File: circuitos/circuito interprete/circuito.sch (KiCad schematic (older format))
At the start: 20 parts, among them IC1 ATMEGA328-P, P1 CONN_5V, P10 CONN_LIM_Y, P11 CONN_E_STOP, P2 CONN_02X03, P3 CONN_EJE_X, P4 CONN_EJE_Y, P5 CONN_EJE_Z, P6 CONN_HUS, P7 CONN_UART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

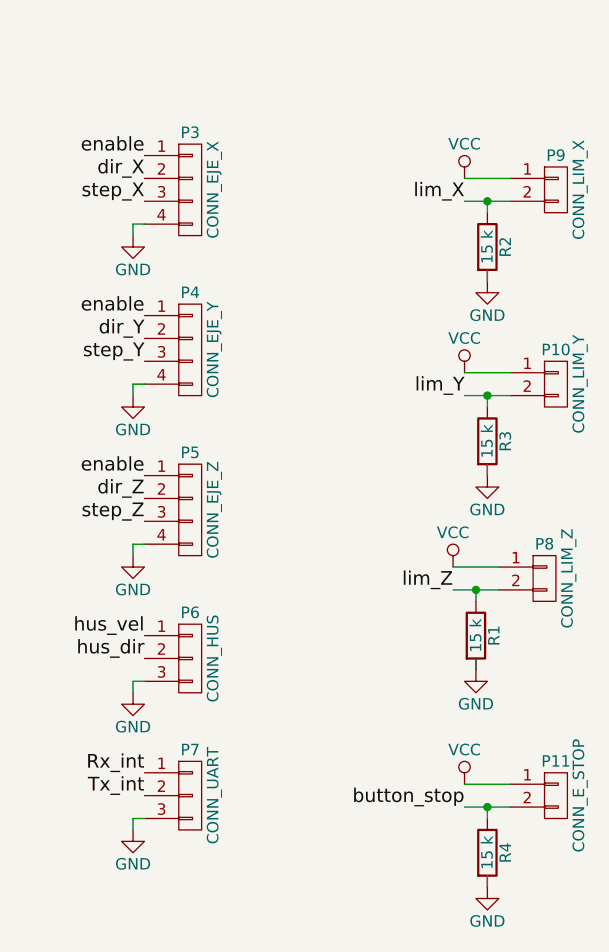
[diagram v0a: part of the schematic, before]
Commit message: cambios en el circuito de pull down.
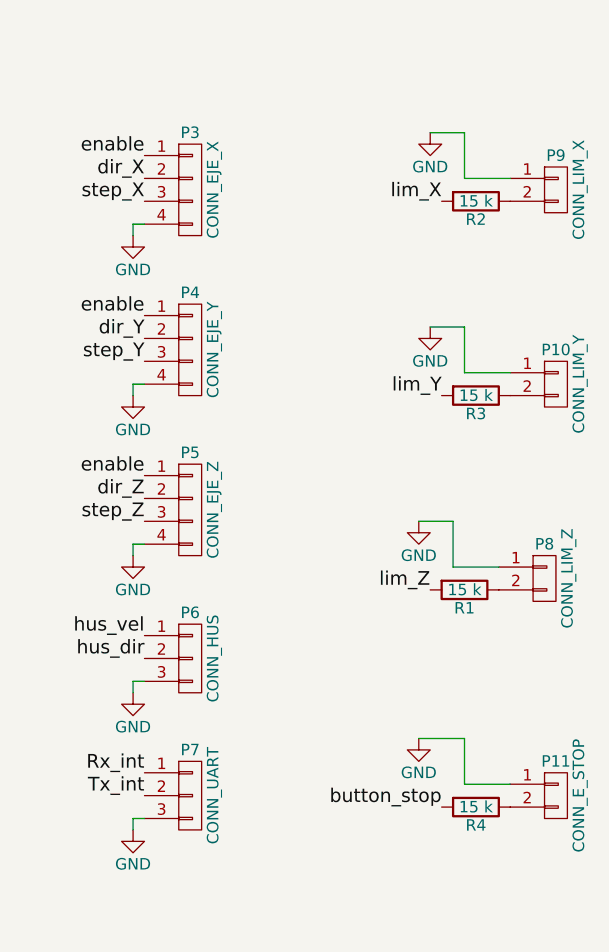
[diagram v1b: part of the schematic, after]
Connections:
- wire segments 56 -> 52
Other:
- moved on the sheet: R1, R2, R3, R4
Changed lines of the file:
@@
 L GND #PWR07
 U 1 1 562ABE39
-P 9350 1900
-F 0 "#PWR07" H 9350 1650 50  0001 C CNN
-F 1 "GND" H 9350 1750 50  0000 C CNN
-F 2 "" H 9350 1900 60  0000 C CNN
-F 3 "" H 9350 1900 60  0000 C CNN
-	1    9350 1900
+P 9100 1250
+F 0 "#PWR07" H 9100 1000 50  0001 C CNN
+F 1 "GND" H 9100 1100 50  0000 C CNN
+F 2 "" H 9100 1250 60  0000 C CNN
+F 3 "" H 9100 1250 60  0000 C CNN
+	1    9100 1250
 	1    0    0    -1
 $EndComp
@@
 L R R2
 U 1 1 562AC0EB
-P 9350 1750
-F 0 "R2" V 9430 1750 50  0000 C CNN
-F 1 "15 k" V 9350 1750 50  0000 C CNN
-F 2 "Resistors_ThroughHole:Resistor_Horizontal_RM10mm" V 9280 1750 30  0001 C CNN
-F 3 "" H 9350 1750 30  0000 C CNN
-	1    9350 1750
-	1    0    0    -1
-$EndComp
-Wire Wire Line
-	9350 1850 9350 1900
-Text Label 9250 1550 2    60   ~ 0
+P 9300 1550
+F 0 "R2" V 9380 1550 50  0000 C CNN
+F 1 "15 k" V 9300 1550 50  0000 C CNN
+F 2 "Resistors_ThroughHole:Resistor_Horizontal_RM10mm" V 9230 1550 30  0001 C CNN
+F 3 "" H 9300 1550 30  0000 C CNN
+	1    9300 1550
+	0    1    1    0
+$EndComp
+Text Label 9150 1550 2    60   ~ 0
 lim_X
-Connection ~ 9350 1550
-Wire Wire Line
-	9350 1600 9350 1550
-Wire Wire Line
-	9250 1550 9450 1550
 $Comp
 L GND #PWR08
 U 1 1 562AE343
-P 9350 2750
-F 0 "#PWR08" H 9350 2500 50  0001 C CNN
-F 1 "GND" H 9350 2600 50  0000 C CNN
-F 2 "" H 9350 2750 60  0000 C CNN
-F 3 "" H 9350 2750 60  0000 C CNN
-	1    9350 2750
+P 9100 2100
+F 0 "#PWR08" H 9100 1850 50  0001 C CNN
+F 1 "GND" H 9100 1950 50  0000 C CNN
+F 2 "" H 9100 2100 60  0000 C CNN
+F 3 "" H 9100 2100 60  0000 C CNN
+	1    9100 2100
 	1    0    0    -1
 $EndComp
@@
 L R R3
 U 1 1 562AE352
-P 9350 2600
-F 0 "R3" V 9430 2600 50  0000 C CNN
-F 1 "15 k" V 9350 2600 50  0000 C CNN
-F 2 "Resistors_ThroughHole:Resistor_Horizontal_RM10mm" V 9280 2600 30  0001 C CNN
-F 3 "" H 9350 2600 30  0000 C CNN
-	1    9350 2600
-	1    0    0    -1
-$EndComp
-Wire Wire Line
-	9350 2700 9350 2750
-Text Label 9250 2400 2    60   ~ 0
+P 9300 2400
+F 0 "R3" V 9380 2400 50  0000 C CNN
+F 1 "15 k" V 9300 2400 50  0000 C CNN
+F 2 "Resistors_ThroughHole:Resistor_Horizontal_RM10mm" V 9230 2400 30  0001 C CNN
+F 3 "" H 9300 2400 30  0000 C CNN
+	1    9300 2400
+	0    1    1    0
+$EndComp
+Text Label 9150 2400 2    60   ~ 0
 lim_Y
-Connection ~ 9350 2400
-Wire Wire Line
-	9350 2450 9350 2400
-Wire Wire Line
-	9250 2400 9450 2400
 $Comp
 L GND #PWR09
 U 1 1 562AE45B
-P 9300 3600
-F 0 "#PWR09" H 9300 3350 50  0001 C CNN
-F 1 "GND" H 9300 3450 50  0000 C CNN
-F 2 "" H 9300 3600 60  0000 C CNN
-F 3 "" H 9300 3600 60  0000 C CNN
-	1    9300 3600
+P 9050 2950
+F 0 "#PWR09" H 9050 2700 50  0001 C CNN
+F 1 "GND" H 9050 2800 50  0000 C CNN
+F 2 "" H 9050 2950 60  0000 C CNN
+F 3 "" H 9050 2950 60  0000 C CNN
+	1    9050 2950
 	1    0    0    -1
 $EndComp
@@
 L R R1
 U 1 1 562AE46A
-P 9300 3450
-F 0 "R1" V 9380 3450 50  0000 C CNN
-F 1 "15 k" V 9300 3450 50  0000 C CNN
-F 2 "Resistors_ThroughHole:Resistor_Horizontal_RM10mm" V 9230 3450 30  0001 C CNN
-F 3 "" H 9300 3450 30  0000 C CNN
-	1    9300 3450
-	1    0    0    -1
-$EndComp
-Wire Wire Line
-	9300 3550 9300 3600
-Text Label 9200 3250 2    60   ~ 0
+P 9250 3250
+F 0 "R1" V 9330 3250 50  0000 C CNN
+F 1 "15 k" V 9250 3250 50  0000 C CNN
+F 2 "Resistors_ThroughHole:Resistor_Horizontal_RM10mm" V 9180 3250 30  0001 C CNN
+F 3 "" H 9250 3250 30  0000 C CNN
+	1    9250 3250
+	0    1    1    0
+$EndComp
+Text Label 9100 3250 2    60   ~ 0
 lim_Z
-Connection ~ 9300 3250
-Wire Wire Line
-	9300 3300 9300 3250
-Wire Wire Line
-	9200 3250 9400 3250
-Text Label 9250 4200 2    60   ~ 0
+Text Label 9150 4200 2    60   ~ 0
 button_stop
 $Comp
 L GND #PWR010
 U 1 1 562B2AB2
-P 9350 4550
-F 0 "#PWR010" H 9350 4300 50  0001 C CNN
-F 1 "GND" H 9350 4400 50  0000 C CNN
-F 2 "" H 9350 4550 60  0000 C CNN
-F 3 "" H 9350 4550 60  0000 C CNN
-	1    9350 4550
+P 9050 3900
+F 0 "#PWR010" H 9050 3650 50  0001 C CNN
+F 1 "GND" H 9050 3750 50  0000 C CNN
+F 2 "" H 9050 3900 60  0000 C CNN
+F 3 "" H 9050 3900 60  0000 C CNN
+	1    9050 3900
 	1    0    0    -1
 $EndComp
@@
 L R R4
 U 1 1 562B2AC0
-P 9350 4400
-F 0 "R4" V 9430 4400 50  0000 C CNN
-F 1 "15 k" V 9350 4400 50  0000 C CNN
-F 2 "Resistors_ThroughHole:Resistor_Horizontal_RM10mm" V 9280 4400 30  0001 C CNN
-F 3 "" H 9350 4400 30  0000 C CNN
-	1    9350 4400
-	1    0    0    -1
-$EndComp
-Wire Wire Line
-	9350 4500 9350 4550
-Connection ~ 9350 4200
-Wire Wire Line
-	9350 4250 9350 4200
+P 9300 4200
+F 0 "R4" V 9380 4200 50  0000 C CNN
+F 1 "15 k" V 9300 4200 50  0000 C CNN
+F 2 "Resistors_ThroughHole:Resistor_Horizontal_RM10mm" V 9230 4200 30  0001 C CNN
+F 3 "" H 9300 4200 30  0000 C CNN
+	1    9300 4200
+	0    1    1    0
+$EndComp
 $Comp
 L GND #PWR011
@@
 	1    0    0    -1
 $EndComp
-$Comp
-L VCC #PWR016
-U 1 1 562D4EF2
-P 9250 1450
-F 0 "#PWR016" H 9250 1300 50  0001 C CNN
-F 1 "VCC" H 9250 1600 50  0000 C CNN
-F 2 "" H 9250 1450 60  0000 C CNN
-F 3 "" H 9250 1450 60  0000 C CNN
-	1    9250 1450
-	1    0    0    -1
-$EndComp
-$Comp
-L VCC #PWR017
-U 1 1 562D4F36
-P 9250 2300
-F 0 "#PWR017" H 9250 2150 50  0001 C CNN
-F 1 "VCC" H 9250 2450 50  0000 C CNN
-F 2 "" H 9250 2300 60  0000 C CNN
-F 3 "" H 9250 2300 60  0000 C CNN
-	1    9250 2300
-	1    0    0    -1
-$EndComp
-$Comp
-L VCC #PWR018
-U 1 1 562D4F7A
-P 9200 3150
-F 0 "#PWR018" H 9200 3000 50  0001 C CNN
-F 1 "VCC" H 9200 3300 50  0000 C CNN
-F 2 "" H 9200 3150 60  0000 C CNN
-F 3 "" H 9200 3150 60  0000 C CNN
-	1    9200 3150
-	1    0    0    -1
-$EndComp
-$Comp
-L VCC #PWR019
-U 1 1 562D4FBE
-P 9250 4100
-F 0 "#PWR019" H 9250 3950 50  0001 C CNN
-F 1 "VCC" H 9250 4250 50  0000 C CNN
-F 2 "" H 9250 4100 60  0000 C CNN
-F 3 "" H 9250 4100 60  0000 C CNN
-	1    9250 4100
-	1    0    0    -1
-$EndComp
 NoConn ~ 5700 2650
 NoConn ~ 5700 2750
@@
 	9250 4100 9450 4100
 Wire Wire Line
-	9250 4200 9450 4200
+	9050 3900 9250 3900
+Wire Wire Line
+	9250 3900 9250 4100
+Wire Wire Line
+	9050 2950 9200 2950
+Wire Wire Line
+	9200 2950 9200 3150
+Wire Wire Line
+	9100 2100 9250 2100
+Wire Wire Line
+	9250 2100 9250 2300
+Wire Wire Line
+	9100 1250 9250 1250
+Wire Wire Line
+	9250 1250 9250 1450
 $EndSCHEMATC

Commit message: adapto graficos para el informe
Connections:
- net button_stop: no longer R4.2
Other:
- moved on the sheet: C1, C2, C3, IC1, P1, P10, P11, P2, P3, P4, P5, P6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
